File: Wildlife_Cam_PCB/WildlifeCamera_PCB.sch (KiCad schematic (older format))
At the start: 28 parts, among them J1 PIR, J2 TRIG, Q1 2N3904, SW1 ON/OFF, U1 BQ24210, U2 ESP32_CAM, U3 MCP1703

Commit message: Updated Schematic
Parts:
- added J?: PROG, symbol Connector_Generic:Conn_01x06
- added J?: PROG_EN, symbol Connector_Generic:Conn_01x02
- added J?: I2C, symbol Connector_Generic:Conn_01x04
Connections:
- net labels added: 5V_PWR, I2C_CLK, I2C_DAT, PROG_EN, U0R, U0T
- wire segments 103 -> 123
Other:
- note added: "I2C Test"
- note added: "Programming"
- note added: "SD Card is changed from 4 bit write to 1 bit write.\nThis frees up 3 x GPIO.\n1 is for External Interrupt\n2 are form I2C - connect to RTC.\nTest this works!!!!"
- moved on the sheet: U2

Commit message: Updated with RTC for filename
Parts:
- D?: symbol device:LED -> WildlifeCamera_PCB-rescue:LED-device
- J1, J2: symbol Connector_Generic:Conn_01x03 -> WildlifeCamera_PCB-rescue:Conn_01x03-Connector_Generic
- J?: symbol Connector_Generic:Conn_01x06 -> WildlifeCamera_PCB-rescue:Conn_01x06-Connector_Generic
- J?: symbol Connector_Generic:Conn_01x02 -> WildlifeCamera_PCB-rescue:Conn_01x02-Connector_Generic
- J?: symbol Connector_Generic:Conn_01x04 -> WildlifeCamera_PCB-rescue:Conn_01x04-Connector_Generic
- Q1, Q?: symbol Device:Q_NPN_BCE -> WildlifeCamera_PCB-rescue:Q_NPN_BCE-Device
- R5, R6, R? (x4): symbol Device:R -> WildlifeCamera_PCB-rescue:R-Device
- SW?: symbol Switch:SW_Push -> WildlifeCamera_PCB-rescue:SW_Push-Switch
- U3: value MCP1703 -> MCP1826 33
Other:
- note added: "Power Supply 3.3V 1A"
- note removed: "Power Supply 3.3V"
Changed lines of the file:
@@
 $EndComp
 $Comp
-L Device:Q_NPN_BCE Q1
+L WildlifeCamera_PCB-rescue:Q_NPN_BCE-Device Q1
 U 1 1 5F433637
 P 2850 6700
@@
 $EndComp
 $Comp
-L Device:R R6
+L WildlifeCamera_PCB-rescue:R-Device R6
 U 1 1 5F433F45
 P 6300 5150
@@
 $EndComp
 $Comp
-L Device:R R5
+L WildlifeCamera_PCB-rescue:R-Device R5
 U 1 1 5F4345CF
 P 2000 6700
@@
 $EndComp
 $Comp
-L Connector_Generic:Conn_01x03 J1
+L WildlifeCamera_PCB-rescue:Conn_01x03-Connector_Generic J1
 U 1 1 5F434B25
 P 1300 6700
@@
 $EndComp
 $Comp
-L power:+3.3V #PWR0103
+L WildlifeCamera_PCB-rescue:+3.3V-power #PWR0103
 U 1 1 5F4389FE
 P 1750 6300
@@
 $EndComp
 $Comp
-L power:+3.3V #PWR0107
+L WildlifeCamera_PCB-rescue:+3.3V-power #PWR0107
 U 1 1 5F43E8AB
 P 8550 3650
@@
 	1750 6800 1750 7050
 $Comp
-L Connector_Generic:Conn_01x03 J2
+L WildlifeCamera_PCB-rescue:Conn_01x03-Connector_Generic J2
 U 1 1 5F455A97
 P 4200 6650
@@
 P 3300 4500
 F 0 "U3" H 3300 4845 60  0000 C CNN
-F 1 "MCP1703" H 3300 4735 60  0000 C CNN
+F 1 "MCP1826 33" H 3300 4735 60  0000 C CNN
 F 2 "REInnovationFootprint:TH_TO92_MCP1703" H 3300 4500 60  0001 C CNN
 F 3 "" H 3300 4500 60  0000 C CNN
@@
 $EndComp
 $Comp
-L power:+3.3V #PWR0110
+L WildlifeCamera_PCB-rescue:+3.3V-power #PWR0110
 U 1 1 5F467366
 P 4250 4400
@@
 Connection ~ 2650 4450
 $Comp
-L device:LED D?
+L WildlifeCamera_PCB-rescue:LED-device D?
 U 1 1 5F4D026C
 P 5850 4700
@@
 	2150 6700 2400 6700
 $Comp
-L Switch:SW_Push SW?
+L WildlifeCamera_PCB-rescue:SW_Push-Switch SW?
 U 1 1 5F4DA4DE
 P 4850 6400
@@
 $EndComp
 $Comp
-L Device:R R?
+L WildlifeCamera_PCB-rescue:R-Device R?
 U 1 1 5F4DF1E6
 P 5400 6650
@@
 $EndComp
 $Comp
-L Device:Q_NPN_BCE Q?
+L WildlifeCamera_PCB-rescue:Q_NPN_BCE-Device Q?
 U 1 1 5F4DF59B
 P 6000 6650
@@
 $EndComp
 $Comp
-L Device:R R?
+L WildlifeCamera_PCB-rescue:R-Device R?
 U 1 1 5F4DFB70
 P 5850 5150
@@
 $EndComp
 $Comp
-L power:+3.3V #PWR?
+L WildlifeCamera_PCB-rescue:+3.3V-power #PWR?
 U 1 1 5F4E0074
 P 5850 4350
@@
 $EndComp
 $Comp
-L power:+3.3V #PWR?
+L WildlifeCamera_PCB-rescue:+3.3V-power #PWR?
 U 1 1 5F4E76B0
 P 4600 6100
@@
 $EndComp
 $Comp
-L Device:R R?
+L WildlifeCamera_PCB-rescue:R-Device R?
 U 1 1 5F4E7ABA
 P 2400 6950
@@
 $EndComp
 $Comp
-L Device:R R?
+L WildlifeCamera_PCB-rescue:R-Device R?
 U 1 1 5F4E826D
 P 5700 6900
@@
 ESP32_CAM Pinout
 Text Notes 2650 4050 0    60   ~ 0
-Power Supply 3.3V
-$Comp
-L Connector_Generic:Conn_01x06 J?
+Power Supply 3.3V 1A
+$Comp
+L WildlifeCamera_PCB-rescue:Conn_01x06-Connector_Generic J?
 U 1 1 5F50D962
 P 10350 3800
@@
 $EndComp
 $Comp
-L Connector_Generic:Conn_01x02 J?
+L WildlifeCamera_PCB-rescue:Conn_01x02-Connector_Generic J?
 U 1 1 5F50EC3E
 P 10350 4350
@@
 	9700 3900 10150 3900
 $Comp
-L Connector_Generic:Conn_01x04 J?
+L WildlifeCamera_PCB-rescue:Conn_01x04-Connector_Generic J?
 U 1 1 5F579B35
 P 9650 5550
@@
 $EndComp
 $Comp
-L power:+3.3V #PWR?
+L WildlifeCamera_PCB-rescue:+3.3V-power #PWR?
 U 1 1 5F57A570
 P 8800 5650
@@
 Text Label 6500 4400 0    60   ~ 0
 I2C_CLK
-Text Label 6500 3900 0    60   ~ 0
+Text Label 6500 4300 0    60   ~ 0
 I2C_DAT
-Wire Wire Line
-	6500 3900 6900 3900
 Wire Wire Line
 	6500 4400 6900 4400
@@
 Text Notes 6550 3300 0    60   ~ 0
 SD Card is changed from 4 bit write to 1 bit write.\nThis frees up 3 x GPIO.\n1 is for External Interrupt\n2 are form I2C - connect to RTC.\nTest this works!!!!
+Wire Wire Line
+	6900 4300 6500 4300
 $EndSCHEMATC

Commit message: PCB update
Sorted most footprints. Put Items in correct places. Not yet routed
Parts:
- removed J?: I2C, symbol WildlifeCamera_PCB-rescue:Conn_01x04-Connector_Generic
- removed U3: MCP1826 33, REInnovationFootprint:TH_TO92_MCP1703, symbol matts_components:MCP1703-Matt
- added D1: ZENER, REInnovationFootprint:TH_Diode_3, symbol matts_components:ZENER
- added J10, J11: PINS2, REInnovationFootprint:TH_SIL-8_large_pads, symbol Connector_Generic:Conn_01x08
- added J3: RTC_DS3231, REInnovationFootprint:TH_RTC_MODULE, symbol WildlifeCamera_PCB-rescue:Conn_01x06-Connector_Generic
- added J6: LOGO1, CuriousElectric3:TCEC_Words_13mm, symbol Connector_Generic:Conn_01x01
- added J7: LOGO2, CuriousElectric3:2019_011_16_CuriousElectricCompany_Logo_Round_Logo_No_words_KiCAD_10mm_PCBLogo, symbol Connector_Generic:Conn_01x01
- added J8: PCB, symbol Connector_Generic:Conn_01x01
- added J9: PV, symbol Connector_Generic:Conn_01x01
- added U1: MCP1826S-3302, REInnovationFootprint:TO220_MCP1826S, symbol matts_components:MCP1826S-3302
- C1: renamed from C3; value 1u -> 1uf; footprint REInnovationFootprint:C1_lg_pad -> REInnovationFootprint:C_1V7_TH
- C2: renamed from C1; footprint REInnovationFootprint:C1_lg_pad -> REInnovationFootprint:C_1V7_TH
- C3: renamed from C4; value 1u -> 1uf; footprint REInnovationFootprint:C1_lg_pad -> REInnovationFootprint:C_1V7_TH
- C4: renamed from C2; footprint REInnovationFootprint:C1_lg_pad -> REInnovationFootprint:C_1V7_TH
- D4: renamed from D?; footprint (none) -> REInnovationFootprint:TH_LED-5MM
- J4: renamed from J?; footprint (none) -> REInnovationFootprint:TH_6x1_CONN
- J5: renamed from J?; footprint (none) -> REInnovationFootprint:TH_Pin_Header_Straight_1x02
- Q1: footprint REInnovationFootprint:TO220_BD135 -> REInnovationFootprint:TO92-EBC_large_pad
- Q2: renamed from Q?; footprint REInnovationFootprint:TO220_BD135 -> REInnovationFootprint:TO92-EBC_large_pad
- SC1: value PV <2W 5.5V -> PV_IN; footprint REInnovationFootprint:PV_130mmx65mm_NoOutline -> REInnovationFootprint:SIL-2_screw_terminal
- SW2: renamed from SW?; value SW_Push -> TRIGGER; footprint (none) -> REInnovationFootprint:SW_PUSH_SMALL_lg_pad
- U3: renamed from U2; footprint (none) -> REInnovationFootprint:ESP32_CAM
- gave numbers to parts that had none: 4
- renumbered R5 to R1, R6 to R10, R1 to R3, R2 to R4, R3 to R5, R4 to R7, U1 to U2
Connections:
- net labels added: ALARM
- wire segments 123 -> 143
- no-connect marks 1 -> 8
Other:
- note added: "RTC DS3231"
- note added: "SD Card is changed from 4 bit write to 1 bit write.\nThis frees up 3 x GPIO.\n1 is for External Interrupt\n2 are form I2C - connect to RTC."
- note added: "Solar PV Input\n<800mA\n<20V DC"
- note removed: "I2C Test"
- note removed: "SD Card is changed from 4 bit write to 1 bit write.\nThis frees up 3 x GPIO.\n1 is for External Interrupt\n2 are form I2C - connect to RTC.\nTest this works!!!!"
- note removed: "Solar PV Input"
- moved on the sheet: D4, J2, Q2, R10, R6, R8, R9, SW2

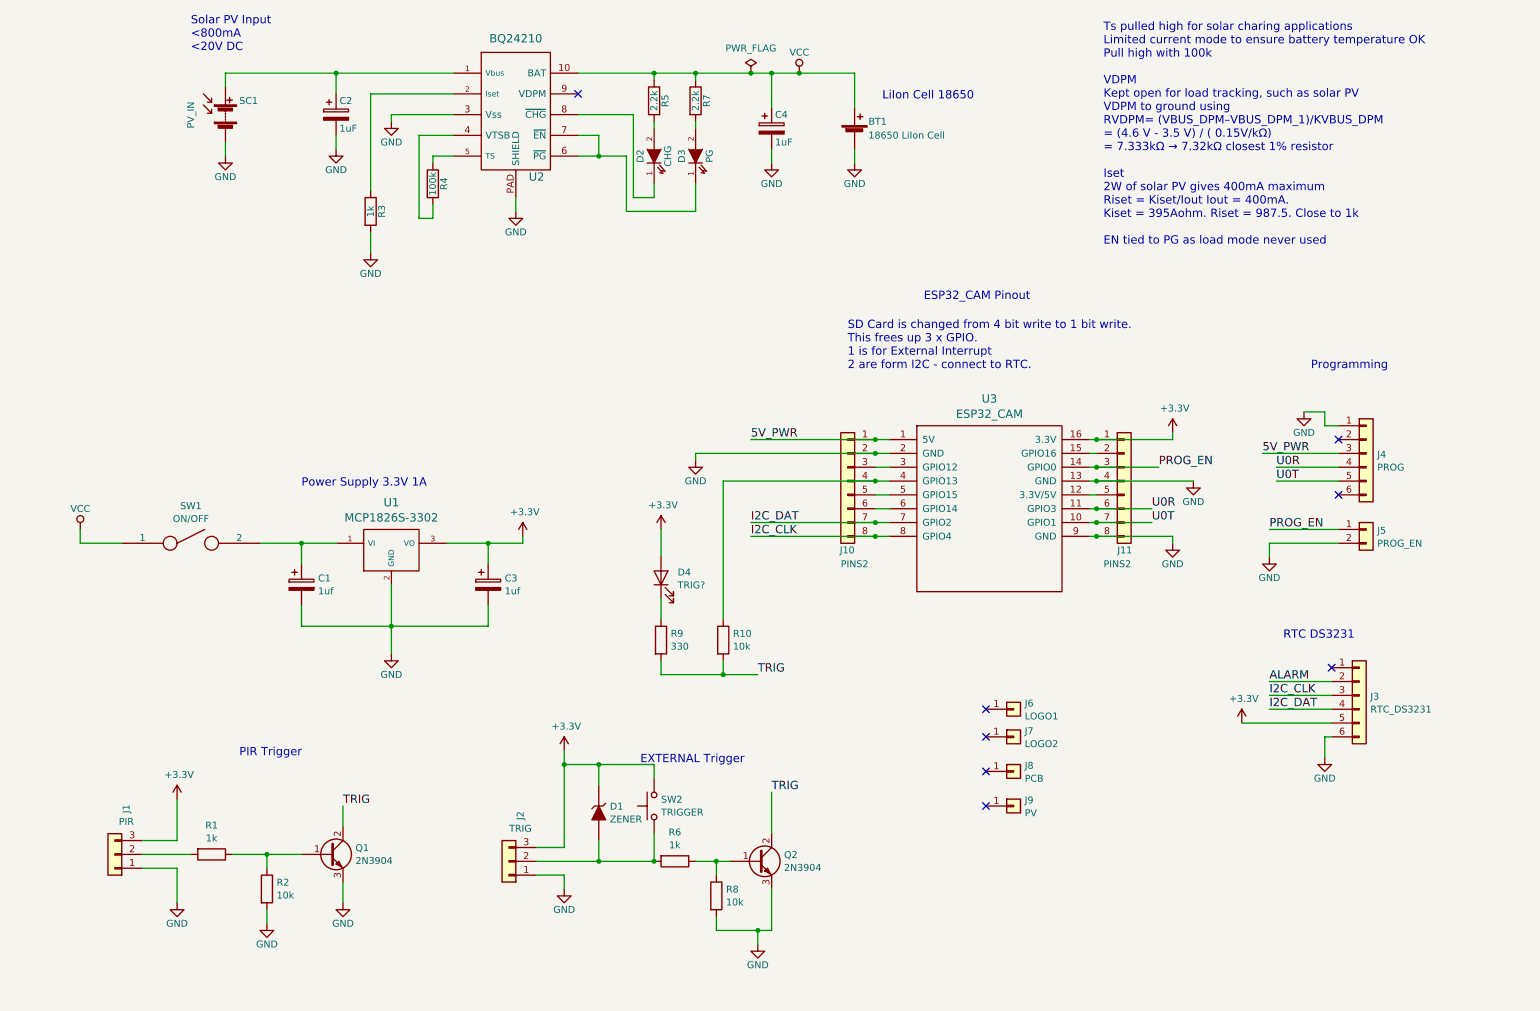
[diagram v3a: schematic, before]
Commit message: Updated firmware with SD error logging
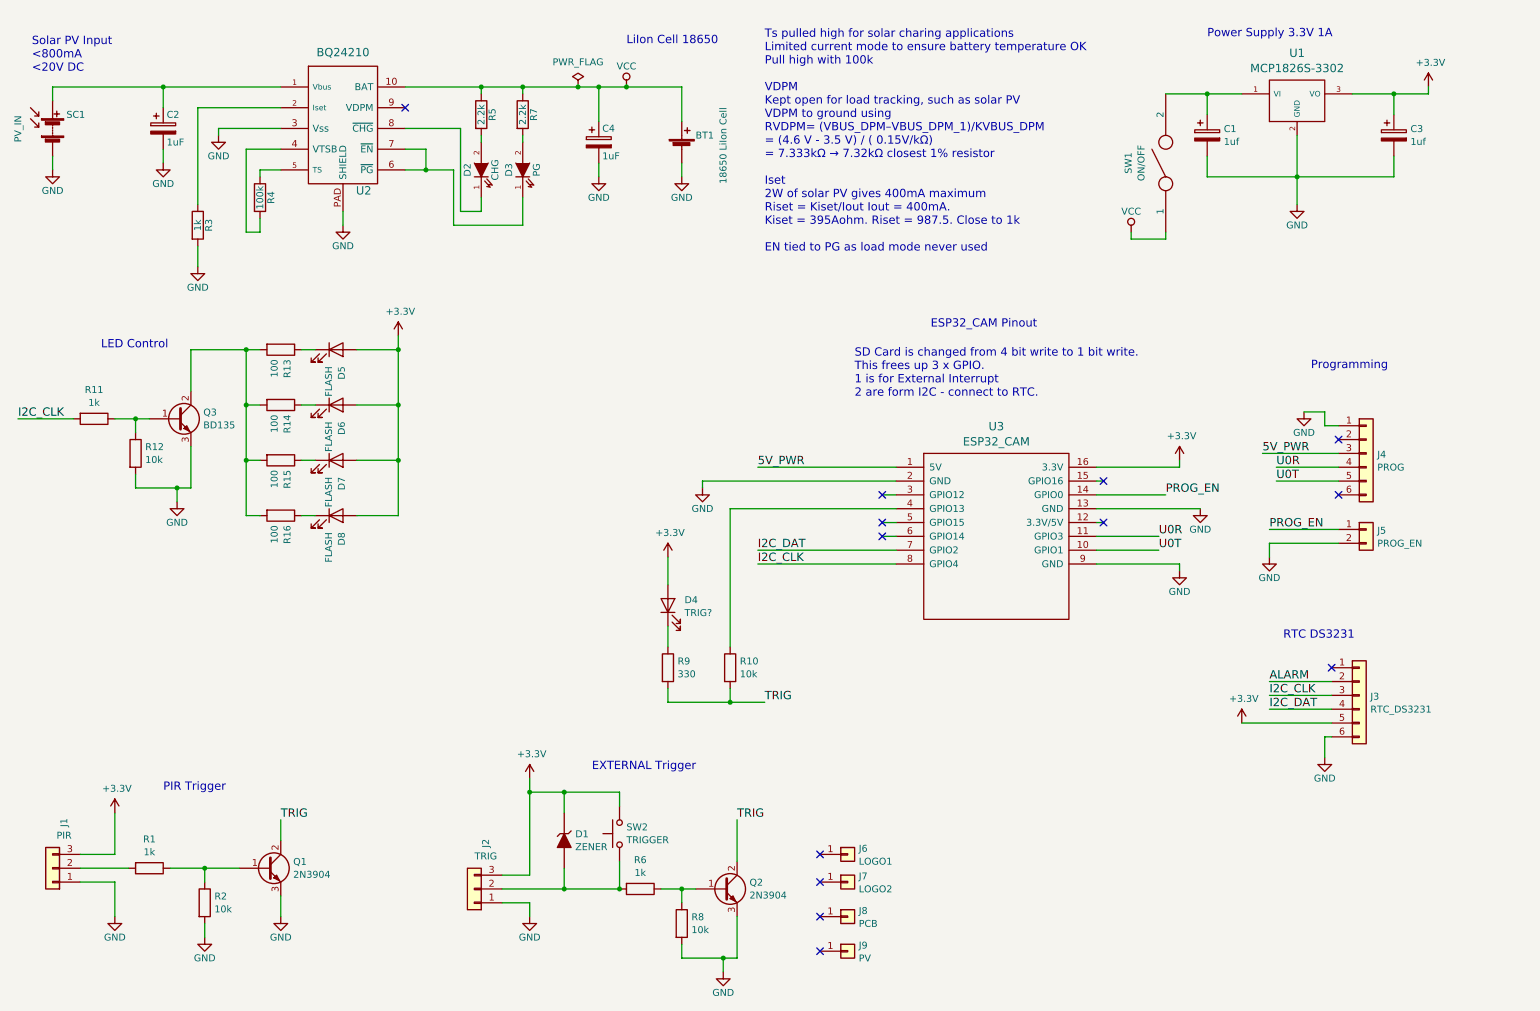
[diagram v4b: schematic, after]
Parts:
- removed J10, J11: PINS2, REInnovationFootprint:TH_SIL-8_large_pads, symbol Connector_Generic:Conn_01x08
- added D5, D6, D7, D8: FLASH, REInnovationFootprint:TH_LED-5MM, symbol WildlifeCamera_PCB-rescue:LED-device
- added Q3: BD135, REInnovationFootprint:TO92-EBC_large_pad, symbol WildlifeCamera_PCB-rescue:Q_NPN_BCE-Device
- added R11: 1k, REInnovationFootprint:TH_Resistor_1, symbol WildlifeCamera_PCB-rescue:R-Device
- added R12: 10k, REInnovationFootprint:TH_Resistor_1, symbol WildlifeCamera_PCB-rescue:R-Device
- added R13, R14, R15, R16: 100, REInnovationFootprint:TH_Resistor_1, symbol WildlifeCamera_PCB-rescue:R-Device
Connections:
- net +3V3: now also D5.1 (A), D6.1 (A), D7.1 (A), D8.1 (A)
- net GND: now also Q3.3 (E), R12.2
- net I2C_CLK: now also R11.2
- new net: Q3.1 (B), R11.1, R12.1
- new net: Q3.2 (C), R13.2, R14.2, R15.2, R16.2
- new net: D5.2 (K), R13.1
- new net: D6.2 (K), R14.1
- new net: D7.2 (K), R15.1
- new net: D8.2 (K), R16.1
- no-connect marks 8 -> 13
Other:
- note added: "LED Control"
- moved on the sheet: BT1, C1, C2, C3, C4, D1, D2, D3, D4, J1, J2, J6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

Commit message: Update of PCB
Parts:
- removed J3: RTC_DS3231, REInnovationFootprint:TH_RTC_MODULE, symbol WildlifeCamera_PCB-rescue:Conn_01x06-Connector_Generic
- added J3: RTC_DS3231, REInnovationFootprint:TH_RTC_MODULE_SM, symbol Connector_Generic:Conn_01x05
- J8: footprint (none) -> REInnovationFootprint:PCB_Wildlife_Cam
- Q3: footprint REInnovationFootprint:TO92-EBC_large_pad -> REInnovationFootprint:TO220_BD135
- SC1: footprint REInnovationFootprint:SIL-2_screw_terminal -> REInnovationFootprint:SIL_2_screw_+_JST_2mm
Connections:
- net +3V3: now also J3.1 (Pin_1); no longer D1.1 (K)
- net GND: now also D1.2 (A), J3.5 (Pin_5)
- net I2C_CLK: now also J3.3 (Pin_3)
- net I2C_DAT: now also J3.2 (Pin_2)
- net at J2.2 (Pin_2), R6.2, SW2.1: now also D1.1 (K); no longer D1.2 (A)
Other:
- moved on the sheet: D1
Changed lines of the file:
@@
 F 0 "SC1" H 950 1550 50  0000 L CNN
 F 1 "PV_IN" V 600 1350 50  0000 L CNN
-F 2 "REInnovationFootprint:SIL-2_screw_terminal" V 850 1510 50  0001 C CNN
+F 2 "REInnovationFootprint:SIL_2_screw_+_JST_2mm" V 850 1510 50  0001 C CNN
 F 3 "" V 850 1510 50  0000 C CNN
 F 4 "~" H 850 1450 60  0000 C CNN "Notes"
@@
 	4100 6850 4300 6850
 Wire Wire Line
-	4100 6950 4550 6950
-Wire Wire Line
-	4550 6950 4950 6950
-Connection ~ 4550 6950
-Wire Wire Line
 	5250 6950 5400 6950
 Wire Wire Line
@@
 Wire Wire Line
 	9700 3900 10150 3900
-$Comp
-L WildlifeCamera_PCB-rescue:+3.3V-power #PWR024
-U 1 1 5F57A570
-P 9450 5750
-F 0 "#PWR024" H 9450 5600 50  0001 C CNN
-F 1 "+3.3V" H 9465 5926 50  0000 C CNN
-F 2 "" H 9450 5750 50  0001 C CNN
-F 3 "" H 9450 5750 50  0001 C CNN
-	1    9450 5750
-	1    0    0    -1
-$EndComp
-$Comp
-L power1:GND #PWR027
-U 1 1 5F57ACA0
-P 10050 6000
-F 0 "#PWR027" H 10050 5750 50  0001 C CNN
-F 1 "GND" H 10050 5850 50  0000 C CNN
-F 2 "" H 10050 6000 50  0000 C CNN
-F 3 "" H 10050 6000 50  0000 C CNN
-	1    10050 6000
-	1    0    0    -1
-$EndComp
 Text Label 5950 4600 0    60   ~ 0
 I2C_CLK
 Text Label 5950 4500 0    60   ~ 0
 I2C_DAT
-Text Label 9650 5650 0    60   ~ 0
-I2C_DAT
-Text Label 9650 5550 0    60   ~ 0
-I2C_CLK
-Wire Wire Line
-	10100 5750 9450 5750
-Wire Wire Line
-	10100 5850 10050 5850
-Wire Wire Line
-	10050 5850 10050 6000
-Wire Wire Line
-	9650 5650 10100 5650
-Wire Wire Line
-	10100 5550 9650 5550
 Text Notes 9750 5150 0    60   ~ 0
 RTC DS3231
@@
 L matts_components:ZENER D1
 U 1 1 5F4F0673
-P 4550 6600
-F 0 "D1" V 4503 6680 50  0000 L CNN
-F 1 "ZENER" V 4596 6680 50  0000 L CNN
-F 2 "REInnovationFootprint:TH_Diode_3" H 4550 6600 50  0001 C CNN
-F 3 "" H 4550 6600 50  0000 C CNN
-	1    4550 6600
+P 4550 7250
+F 0 "D1" V 4503 7330 50  0000 L CNN
+F 1 "ZENER" V 4596 7330 50  0000 L CNN
+F 2 "REInnovationFootprint:TH_Diode_3" H 4550 7250 50  0001 C CNN
+F 3 "" H 4550 7250 50  0000 C CNN
+	1    4550 7250
 	0    1    1    0
 $EndComp
 Wire Wire Line
 	4950 6350 4950 6250
-Wire Wire Line
-	4950 6250 4550 6250
 Wire Wire Line
 	4300 6250 4300 6850
@@
 Connection ~ 4300 6250
 Wire Wire Line
-	4550 6400 4550 6250
-Connection ~ 4550 6250
-Wire Wire Line
-	4550 6250 4300 6250
-Wire Wire Line
 	4950 6750 4950 6950
 Connection ~ 4950 6950
-Wire Wire Line
-	4550 6800 4550 6950
-$Comp
-L WildlifeCamera_PCB-rescue:Conn_01x06-Connector_Generic J3
-U 1 1 5F510D1E
-P 10300 5550
-F 0 "J3" H 10380 5542 50  0000 L CNN
-F 1 "RTC_DS3231" H 10380 5449 50  0000 L CNN
-F 2 "REInnovationFootprint:TH_RTC_MODULE" H 10300 5550 50  0001 C CNN
-F 3 "~" H 10300 5550 50  0001 C CNN
-	1    10300 5550
-	1    0    0    -1
-$EndComp
 NoConn ~ 10150 3700
 NoConn ~ 10150 4100
-Text Label 9650 5450 0    60   ~ 0
-ALARM
-Wire Wire Line
-	9650 5450 10100 5450
-NoConn ~ 10100 5350
 $Comp
 L Connector_Generic:Conn_01x01 J7
@@
 F 0 "J8" H 6680 7192 50  0000 L CNN
 F 1 "PCB" H 6680 7099 50  0000 L CNN
-F 2 "" H 6600 7150 50  0001 C CNN
+F 2 "REInnovationFootprint:PCB_Wildlife_Cam" H 6600 7150 50  0001 C CNN
 F 3 "~" H 6600 7150 50  0001 C CNN
 	1    6600 7150
@@
 F 0 "Q3" H 1940 3597 50  0000 L CNN
 F 1 "BD135" H 1940 3504 50  0000 L CNN
-F 2 "REInnovationFootprint:TO92-EBC_large_pad" H 1950 3650 50  0001 C CNN
+F 2 "REInnovationFootprint:TO220_BD135" H 1950 3650 50  0001 C CNN
 F 3 "~" H 1750 3550 50  0001 C CNN
 	1    1750 3550
@@
 Wire Wire Line
 	8900 2250 8900 2200
+$Comp
+L Connector_Generic:Conn_01x05 J3
+U 1 1 5F9E542B
+P 10300 5700
+F 0 "J3" H 10380 5742 50  0000 L CNN
+F 1 "RTC_DS3231" H 10380 5651 50  0000 L CNN
+F 2 "REInnovationFootprint:TH_RTC_MODULE_SM" H 10300 5700 50  0001 C CNN
+F 3 "~" H 10300 5700 50  0001 C CNN
+	1    10300 5700
+	1    0    0    -1
+$EndComp
+$Comp
+L WildlifeCamera_PCB-rescue:+3.3V-power #PWR024
+U 1 1 5F9E59FA
+P 9950 5500
+F 0 "#PWR024" H 9950 5350 50  0001 C CNN
+F 1 "+3.3V" H 9965 5676 50  0000 C CNN
+F 2 "" H 9950 5500 50  0001 C CNN
+F 3 "" H 9950 5500 50  0001 C CNN
+	1    9950 5500
+	1    0    0    -1
+$EndComp
+$Comp
+L power1:GND #PWR027
+U 1 1 5F9E5C64
+P 9950 5900
+F 0 "#PWR027" H 9950 5650 50  0001 C CNN
+F 1 "GND" H 9950 5750 50  0000 C CNN
+F 2 "" H 9950 5900 50  0000 C CNN
+F 3 "" H 9950 5900 50  0000 C CNN
+	1    9950 5900
+	1    0    0    -1
+$EndComp
+Text Label 9550 5700 0    60   ~ 0
+I2C_CLK
+Text Label 9550 5600 0    60   ~ 0
+I2C_DAT
+NoConn ~ 10100 5800
+Wire Wire Line
+	10100 5900 9950 5900
+Wire Wire Line
+	9950 5500 10100 5500
+Wire Wire Line
+	10100 5600 9550 5600
+Wire Wire Line
+	9550 5700 10100 5700
+Wire Wire Line
+	4100 6950 4550 6950
+Wire Wire Line
+	4300 6250 4950 6250
+Wire Wire Line
+	4550 7050 4550 6950
+Connection ~ 4550 6950
+Wire Wire Line
+	4550 6950 4950 6950
+$Comp
+L power1:GND #PWR0101
+U 1 1 5FA7F2FD
+P 4550 7550
+F 0 "#PWR0101" H 4550 7300 50  0001 C CNN
+F 1 "GND" H 4550 7400 50  0000 C CNN
+F 2 "" H 4550 7550 50  0000 C CNN
+F 3 "" H 4550 7550 50  0000 C CNN
+	1    4550 7550
+	1    0    0    -1
+$EndComp
+Wire Wire Line
+	4550 7550 4550 7450
 $EndSCHEMATC
